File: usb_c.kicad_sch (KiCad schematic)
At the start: 5 parts, among them J1 USB_C_Receptacle_USB2.0, U4 USBLC6-2SC6

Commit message: laid out stuff
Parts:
- added TP1: 5260 (Red), TestPoint:TestPoint_Keystone_5000-5004_Miniature, symbol Connector:TestPoint
- added TP3: 5261 (Black), TestPoint:TestPoint_Keystone_5000-5004_Miniature, symbol Connector:TestPoint
- U4: AVAILABILITY In Stock -> (none); Availability In Stock -> (none); Check_prices https://www.snapeda.com/parts/USBLC6-2SC6/STMicroelectronic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 -> (none); DESCRIPTION 17V Clamp 5A (8/20µs) Ipp Tvs Diode Surface Mount SOT-23-6 -> (none); MF STMicroelectronics -> (none); MP USBLC6-2SC6 -> (none); PACKAGE SOT-23-6 STMicroelectronics -> (none); PRICE None -> (none); PURCHASE-URL https://pricing.snapeda.com/search/part/USBLC6-2SC6/?ref=eda -> (none); Package SOT-23-6 STMicroelectronics -> (none); Price None -> (none); Purchase-URL https://www.snapeda.com/api/url_track_click_mouser/?unipart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 -> (none); SnapEDA_Link https://www.snapeda.com/parts/USBLC6-2SC6/STMicroelectronic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 -> (none)
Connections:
- net GND: now also TP3.1
- net USB_N: now also U4.1; no longer U4.4
- net USB_P: now also U4.3; no longer U4.6
- net VBUS: now also TP1.1
- net at J1.A6 (D+), J1.B6 (D+): now also U4.4; no longer U4.1
- net at J1.A7 (D-), J1.B7 (D-): now also U4.6; no longer U4.3
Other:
- moved on the sheet: C8, U4

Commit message: neat-ified schematics
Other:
- company: (none) -> The Art and Science of PCB Design
- title: (none) -> RGB LED Driver Demo Board
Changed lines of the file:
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@@
   (paper "USLetter")
   (title_block
+    (title "RGB LED Driver Demo Board")
     (date "2024-01-01")
     (rev "A01")
+    (company "The Art and Science of PCB Design")
   )
   (junction (at 130.81 49.53) (diameter 0) (color 0 0 0 0)

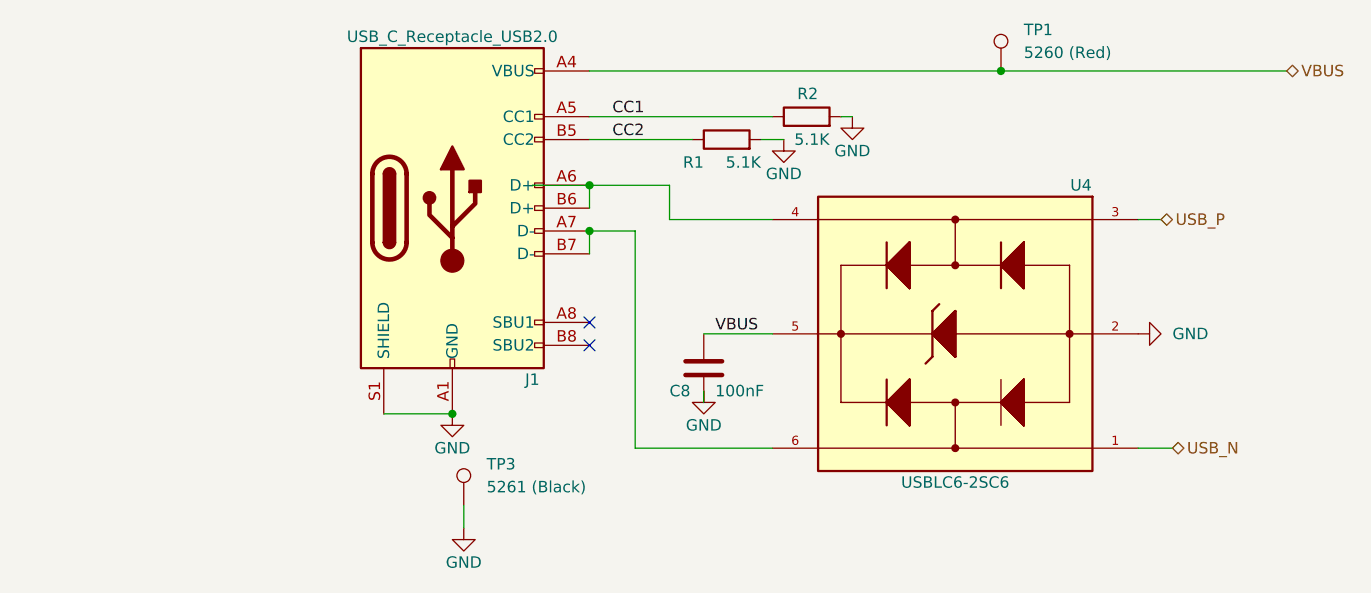
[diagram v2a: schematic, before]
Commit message: Added annotations, BOM count reduction
LED indicator resistors edited to save on BOM count

schematics made more neat, added some labels
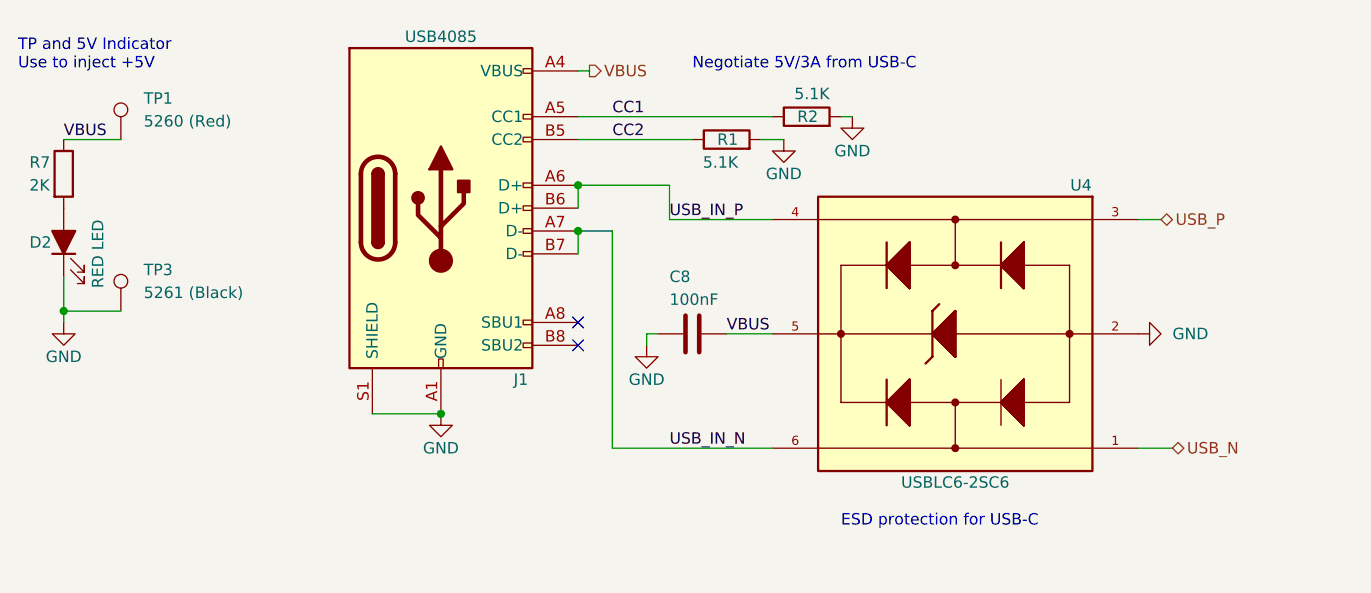
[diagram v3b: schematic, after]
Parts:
- added D2: RED LED, LED_SMD:LED_0805_2012Metric_Pad1.15x1.40mm_HandSolder, symbol Device:LED_Filled
- added R7: 2K, Resistor_SMD:R_0805_2012Metric_Pad1.20x1.40mm_HandSolder, symbol Device:R
- J1: value USB_C_Receptacle_USB2.0 -> USB4085
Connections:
- net GND: now also D2.1 (K)
- net VBUS: now also R7.1
- net USB_IN_P: now reaches J1.A6 (D+), J1.B6 (D+), U4.4
- net USB_IN_N: now reaches J1.A7 (D-), J1.B7 (D-), U4.6
- new net: D2.2 (A), R7.2
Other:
- note added: "ESD protection for USB-C"
- note added: "Negotiate 5V/3A from USB-C"
- note added: "TP and 5V Indicator Use to inject +5V"
- moved on the sheet: C8, J1, TP3

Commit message: added digikey PNs
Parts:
- C8: Digikey PN (none) -> 1276-1003-1-ND; MPN (none) -> CL21B104KBCNNNC
- D2: Digikey PN (none) -> 160-1427-1-ND; MPN (none) -> LTST-C171KRKT
- J1: Digikey PN (none) -> 2073-USB4085-GF-ACT-ND; MPN (none) -> USB4085-GF-A
- R7: MPN (none) -> 0805W8F2001
- TP1: Digikey PN (none) -> 36-5260-ND; MPN (none) -> 5260
- TP3: Digikey PN (none) -> 36-5261-ND; MPN (none) -> 5261
- U4: Digikey PN (none) -> 497-5235-1-ND; MPN (none) -> USBLC6-2SC6
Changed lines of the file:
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@@
       (effects (font (size 1.27 1.27)) hide)
     )
-    (property "Digikey PN" "" (at 26.67 68.58 0)
+    (property "Digikey PN" "160-1427-1-ND" (at 26.67 68.58 0)
+      (effects (font (size 1.27 1.27)) hide)
+    )
+    (property "MPN" "LTST-C171KRKT" (at 26.67 68.58 0)
       (effects (font (size 1.27 1.27)) hide)
     )
@@
       (effects (font (size 1.27 1.27)) hide)
     )
+    (property "MPN" "0805W8F2001" (at 26.67 60.96 0)
+      (effects (font (size 1.27 1.27)) hide)
+    )
     (pin "1")
     (pin "2")
@@
       (effects (font (size 1.27 1.27)) hide)
     )
-    (property "Digikey PN" "" (at 96.52 78.74 0)
+    (property "Digikey PN" "1276-1003-1-ND" (at 96.52 78.74 0)
+      (effects (font (size 1.27 1.27)) hide)
+    )
+    (property "MPN" "CL21B104KBCNNNC" (at 96.52 78.74 0)
       (effects (font (size 1.27 1.27)) hide)
     )
@@
       (effects (font (size 1.27 1.27)) hide)
     )
-    (property "Digikey PN" "" (at 33.02 76.2 0)
+    (property "Digikey PN" "36-5261-ND" (at 33.02 76.2 0)
+      (effects (font (size 1.27 1.27)) hide)
+    )
+    (property "MPN" "5261" (at 33.02 76.2 0)
       (effects (font (size 1.27 1.27)) hide)
     )
@@
       (effects (font (size 1.27 1.27)) hide)
     )
-    (property "Digikey PN" "" (at 33.02 57.15 0)
+    (property "Digikey PN" "36-5260-ND" (at 33.02 57.15 0)
+      (effects (font (size 1.27 1.27)) hide)
+    )
+    (property "MPN" "5260" (at 33.02 57.15 0)
       (effects (font (size 1.27 1.27)) hide)
     )
@@
       (effects (font (size 1.27 1.27)) hide)
     )
-    (property "Digikey PN" "" (at 125.73 78.74 0)
+    (property "Digikey PN" "497-5235-1-ND" (at 125.73 78.74 0)
+      (effects (font (size 1.27 1.27)) hide)
+    )
+    (property "MPN" "USBLC6-2SC6" (at 125.73 78.74 0)
       (effects (font (size 1.27 1.27)) hide)
     )
@@
       (effects (font (size 1.27 1.27)) hide)
     )
-    (property "Digikey PN" "" (at 68.58 64.77 0)
-      (effects (font (size 1.27 1.27)) hide)
-    )
+    (property "Digikey PN" "2073-USB4085-GF-ACT-ND" (at 68.58 64.77 0)
+      (effects (font (size 1.27 1.27)) hide)
+    )
+    (property "MPN" "USB4085-GF-A" (at 68.58 64.77 0)
+      (effects (font (size 1.27 1.27)) hide)
+    )

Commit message: added digikey PNs to all devices
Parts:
- R1, R2: Digikey PN (none) -> RMCF0805FT5K10CT-ND; MPN (none) -> RMCF0805FT5K10
- R7: Digikey PN (none) -> RMCF0805FT2K00CT-ND; MPN 0805W8F2001 -> RMCF0805FT2K00
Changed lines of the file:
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@@
       (effects (font (size 1.27 1.27)) hide)
     )
-    (property "Digikey PN" "" (at 26.67 60.96 0)
-      (effects (font (size 1.27 1.27)) hide)
-    )
-    (property "MPN" "0805W8F2001" (at 26.67 60.96 0)
+    (property "Digikey PN" "RMCF0805FT2K00CT-ND" (at 26.67 60.96 0)
+      (effects (font (size 1.27 1.27)) hide)
+    )
+    (property "MPN" "RMCF0805FT2K00" (at 26.67 60.96 0)
       (effects (font (size 1.27 1.27)) hide)
     )
@@
       (effects (font (size 1.27 1.27)) hide)
     )
-    (property "Digikey PN" "" (at 100.33 57.15 0)
+    (property "Digikey PN" "RMCF0805FT5K10CT-ND" (at 100.33 57.15 0)
+      (effects (font (size 1.27 1.27)) hide)
+    )
+    (property "MPN" "RMCF0805FT5K10" (at 100.33 57.15 0)
       (effects (font (size 1.27 1.27)) hide)
     )
@@
       (effects (font (size 1.27 1.27)) hide)
     )
-    (property "Digikey PN" "" (at 109.22 54.61 0)
-      (effects (font (size 1.27 1.27)) hide)
-    )
+    (property "Digikey PN" "RMCF0805FT5K10CT-ND" (at 109.22 54.61 0)
+      (effects (font (size 1.27 1.27)) hide)
+    )
+    (property "MPN" "RMCF0805FT5K10" (at 109.22 54.61 0)
+      (effects (font (size 1.27 1.27)) hide)
+    )
